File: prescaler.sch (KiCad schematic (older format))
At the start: 33 parts, among them J1 Conn_Coaxial_x2, J2 Conn_01x04, J3 Conn_Coaxial_x2, U1 HMC705LP4, U2 HMC705LP4

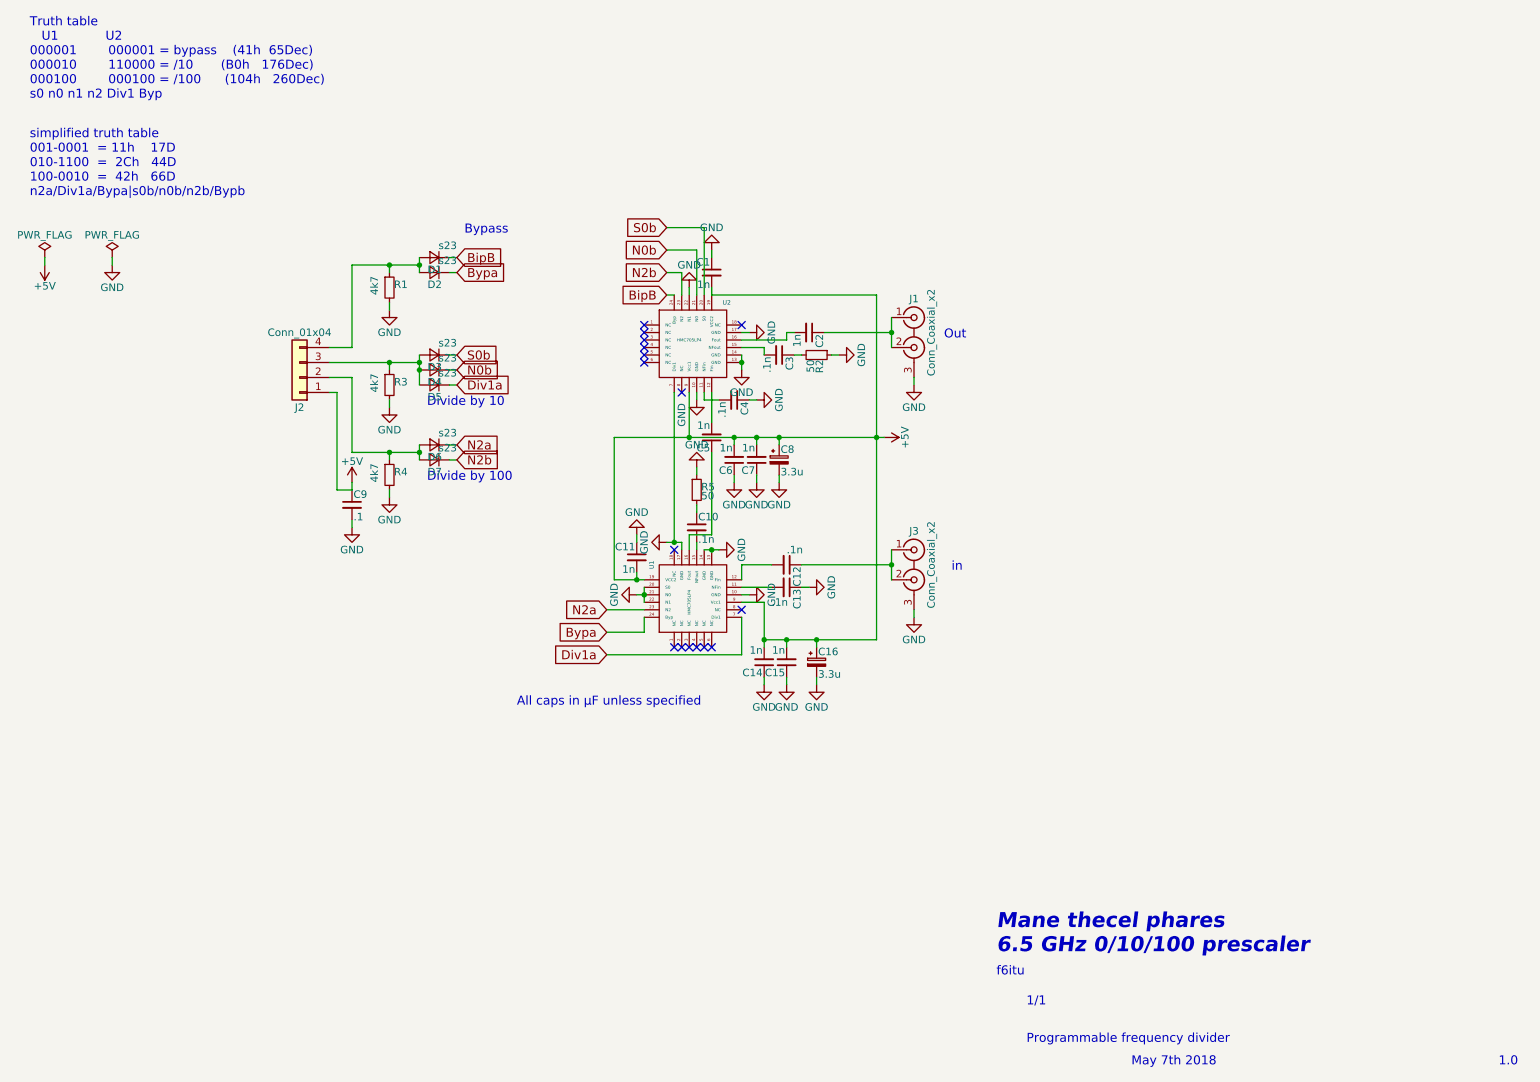
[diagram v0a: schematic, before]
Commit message: voltage reg. added, switching not inclued
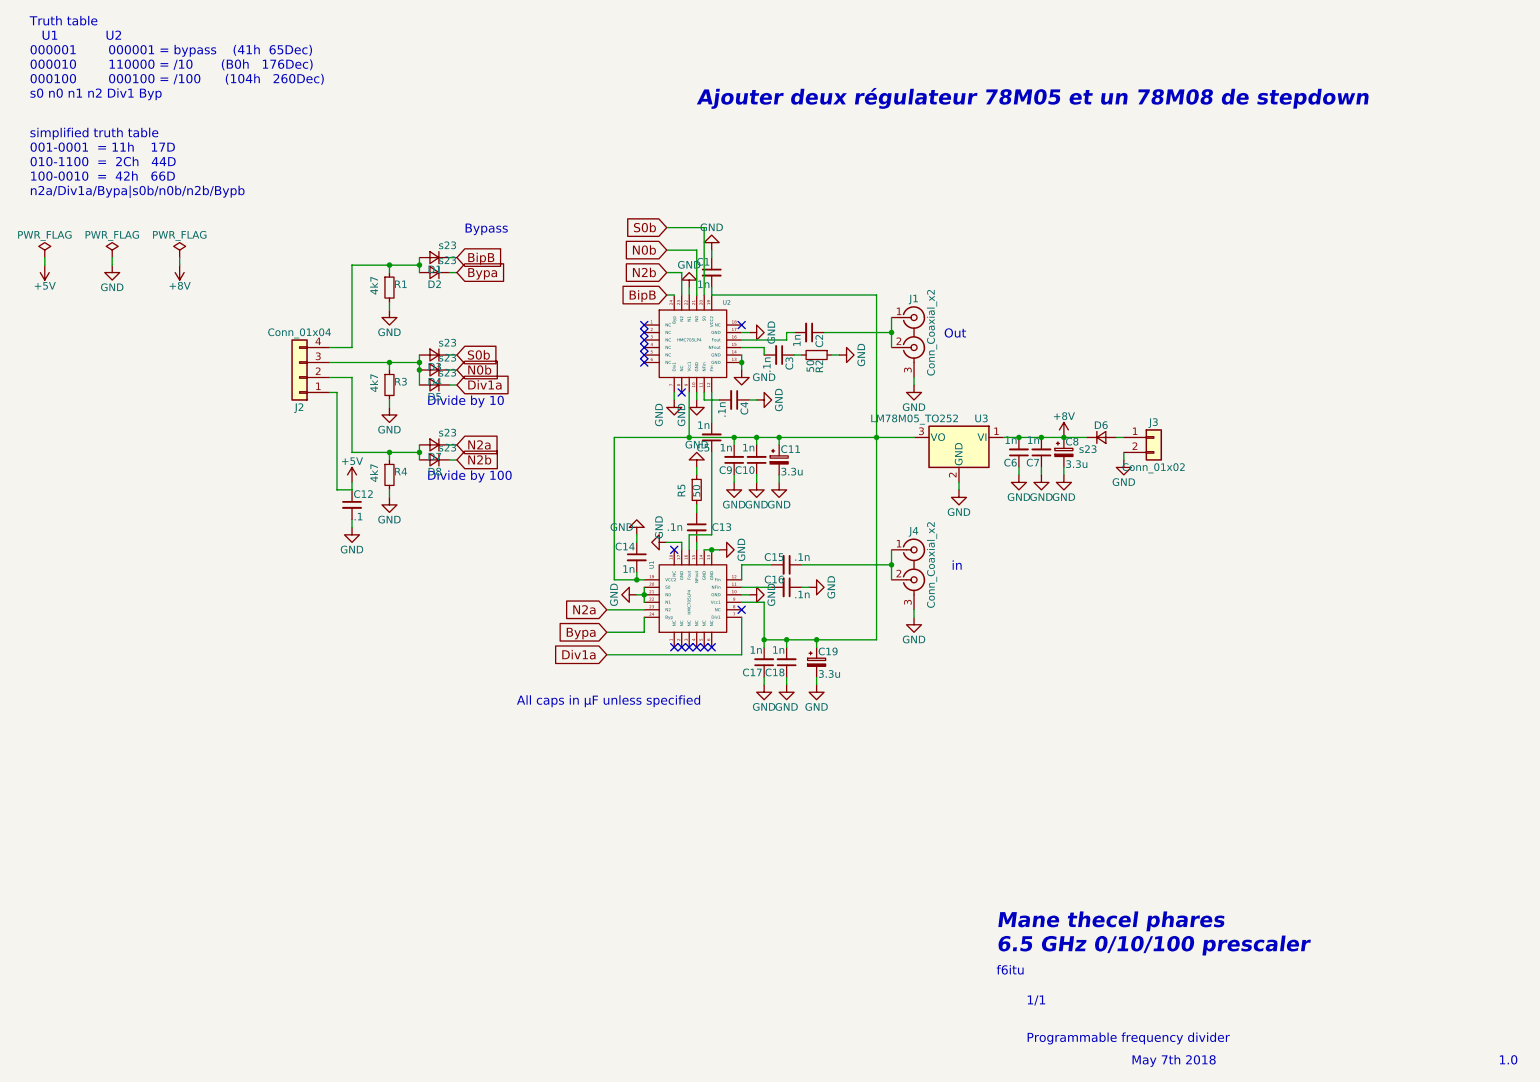
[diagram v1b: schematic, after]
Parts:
- added C6, C7: 1n, symbol C_Small
- added C8: 3.3u, symbol CP_Small
- added D6: s23, symbol D_Small
- added J3: Conn_01x02, symbol Conn_01x02
- added U3: LM78M05_TO252, Package_TO_SOT_SMD:TO-252-2, symbol LM78M05_TO252
- renumbered C7 to C10, C8 to C11, C9 to C12, C10 to C13, C11 to C14, C12 to C15, C13 to C16, C14 to C17, C15 to C18, C16 to C19, C6 to C9, D6 to D7, D7 to D8, J3 to J4
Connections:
- net +5V: no longer C1.2, C10.2, C11.1, C14.2, C17.2, C18.2, C19.1, C9.2, U1.19 (VCC2), U1.9 (Vcc1), U2.19 (VCC2), U2.9 (Vcc1)
- net GND: now also C6.1, C7.1, C8.2, J3.2 (Pin_2), U3.2 (GND)
- new net: C1.2, C10.2, C11.1, C14.2, C17.2, C18.2, C19.1, C9.2, U1.19 (VCC2), U1.9 (Vcc1), U2.19 (VCC2), U2.9 (Vcc1), U3.3 (VO)
- new net: D6.2 (A), J3.1 (Pin_1)
- new net +8V: C6.2, C7.2, C8.1, D6.1 (K), U3.1 (VI)
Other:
- note added: "Ajouter deux régulateur 78M05 et un 78M08 de stepdown"
